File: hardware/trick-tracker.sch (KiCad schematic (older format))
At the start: 58 parts, among them J1 USB4105-GF-A, J2 S2B-PH-K, J3 QWiiC, J4 MEM2051-00-195-00-A, J6 QWiiC, P1 SMTB-1240-S-R, U1 MS88SF2, U2 DPS368XTSA1, U3 LSM9DS1, U4 MCP73831/OT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

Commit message: Finished trace routing
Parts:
- J4: value MEM2051-00-195-00-A -> MEM2061-01-188-00-A
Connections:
- no-connect marks 10 -> 9
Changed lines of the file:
@@
 Text Label 3400 6050 2    50   ~ 0
 D-
-NoConn ~ 3100 6450
 $Comp
 L power:GND #PWR0104
@@
 P 2150 4500
 F 0 "J4" H 2150 5067 50  0000 C CNN
-F 1 "MEM2051-00-195-00-A" H 2150 4976 50  0000 C CNN
+F 1 "MEM2061-01-188-00-A" H 2150 4976 50  0000 C CNN
 F 2 "MEM2061-01-188-00-A_REVA:GCT_MEM2061-01-188-00-A_REVA" H 2150 4500 50  0001 L BNN
 F 3 "" H 2150 4500 50  0001 L BNN

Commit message: Small adjustments + rounded corners + BOM HTML
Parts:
- H1, H2, H3, H4: footprint MountingHole:MountingHole_2.5mm -> MountingHole:MountingHole_2.5mm_Pad_Via
- J1: Alternative (none) -> TYPE-C-31-M-12; MANUFACTURER GCT -> (none); MAXIMUM_PACKAGE_HEIGHT 3.31 mm -> (none); PARTREV A3 -> (none); STANDARD Manufacturer Recommendations -> (none)
- J4: MANUFACTURER GCT -> (none)
- S1, S2: Arrow Part Number EVQ-PUA02K -> (none); Arrow Price/Stock https://www.arrow.com/en/products/evq-pua02k/panasonic -> (none); Height 1.95 -> (none); Manufacturer_Name Panasonic -> (none); Manufacturer_Part_Number EVQ-PUA02K -> (none); Mouser Part Number 667-EVQ-PUA02K -> (none); Mouser Price/Stock https://www.mouser.co.uk/ProductDetail/Panasonic/EVQ-PUA02K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 -> (none)
- S3: Manufacturer_Name Wurth Elektronik -> (none); Manufacturer_Part_Number 450405020524 -> (none); Mouser Part Number 710-450405020524 -> (none); Mouser Price/Stock https://www.mouser.co.uk/ProductDetail/Wurth-Elektronik/450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 -> (none)
- U2: Field4 Infineon Technologies -> (none); Field5 None -> (none); Field6 Unavailable -> (none); Field7 DPS368XTSA1 -> (none); Field8 Package dimensions: 8-pin LGA, 2.0 x 2.5 x 1.1 mm3 | Operat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 -> (none)
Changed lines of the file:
@@
 F 2 "DPS368XTSA1:XDCR_DPS368XTSA1" H 5600 4200 50  0001 L BNN
 F 3 "VFLGA-8 Infineon Technologies" H 5600 4200 50  0001 L BNN
-F 4 "Infineon Technologies" H 5600 4200 50  0001 L BNN "Field4"
-F 5 "None" H 5600 4200 50  0001 L BNN "Field5"
-F 6 "Unavailable" H 5600 4200 50  0001 L BNN "Field6"
-F 7 "DPS368XTSA1" H 5600 4200 50  0001 L BNN "Field7"
-F 8 "Package dimensions: 8-pin LGA, 2.0 x 2.5 x 1.1 mm3 | Operation range: Pressure: 3001200 hPa Temperature: -4085C | Precision: 0.002 hPa _or 0.02 m_ | Rel. accuracy: 0.06 hPa _or 0.5 m_ | Abs. accuracy: 1 hPa _or 8 m_ | Temperature accuracy: 0.5C | Avg. current consumption: 1.7 A_pressure measurement_ @1Hzsampling rate, standby: 0.5 A. | Integrated FIFO | Interface: I2C and SPI_both with optional interrupt_" H 5600 4200 50  0001 L BNN "Field8"
 	1    5600 4200
 	1    0    0    -1
@@
 F 2 "USB4105-GF-A:GCT_USB4105-GF-A" H 2300 6050 50  0001 L BNN
 F 3 "" H 2300 6050 50  0001 L BNN
-F 4 "A3" H 2300 6050 50  0001 L BNN "PARTREV"
-F 5 "3.31 mm" H 2300 6050 50  0001 L BNN "MAXIMUM_PACKAGE_HEIGHT"
-F 6 "Manufacturer Recommendations" H 2300 6050 50  0001 L BNN "STANDARD"
-F 7 "GCT" H 2300 6050 50  0001 L BNN "MANUFACTURER"
+F 4 "TYPE-C-31-M-12" H 2300 6100 50  0001 C CNN "Alternative"
 	1    2300 6050
 	1    0    0    -1
@@
 F 3 "https://www.mouser.in/ProductDetail/Panasonic/EVQ-PUA02K?qs=%2Fha2pyFadujMSX8lHuHLeTqtnZtxLpuLygd0%252BejhC2g%3D" H 6000 6750 50  0001 L CNN
 F 4 "Tactile Switches SIDE PUSH 2.2NF 4.7x3.2x1.65mm" H 6000 6650 50  0001 L CNN "Description"
-F 5 "1.95" H 6000 6550 50  0001 L CNN "Height"
-F 6 "Panasonic" H 6000 6450 50  0001 L CNN "Manufacturer_Name"
-F 7 "EVQ-PUA02K" H 6000 6350 50  0001 L CNN "Manufacturer_Part_Number"
-F 8 "667-EVQ-PUA02K" H 6000 6250 50  0001 L CNN "Mouser Part Number"
-F 9 "https://www.mouser.co.uk/ProductDetail/Panasonic/EVQ-PUA02K?qs=whhzBCqEXCvFsgipcL1tig%3D%3D" H 6000 6150 50  0001 L CNN "Mouser Price/Stock"
-F 10 "EVQ-PUA02K" H 6000 6050 50  0001 L CNN "Arrow Part Number"
-F 11 "https://www.arrow.com/en/products/evq-pua02k/panasonic" H 6000 5950 50  0001 L CNN "Arrow Price/Stock"
 	1    4950 6750
 	1    0    0    -1
@@
 F 3 "https://www.mouser.in/ProductDetail/Panasonic/EVQ-PUA02K?qs=%2Fha2pyFadujMSX8lHuHLeTqtnZtxLpuLygd0%252BejhC2g%3D" H 6000 7400 50  0001 L CNN
 F 4 "Tactile Switches SIDE PUSH 2.2NF 4.7x3.2x1.65mm" H 6000 7300 50  0001 L CNN "Description"
-F 5 "1.95" H 6000 7200 50  0001 L CNN "Height"
-F 6 "Panasonic" H 6000 7100 50  0001 L CNN "Manufacturer_Name"
-F 7 "EVQ-PUA02K" H 6000 7000 50  0001 L CNN "Manufacturer_Part_Number"
-F 8 "667-EVQ-PUA02K" H 6000 6900 50  0001 L CNN "Mouser Part Number"
-F 9 "https://www.mouser.co.uk/ProductDetail/Panasonic/EVQ-PUA02K?qs=whhzBCqEXCvFsgipcL1tig%3D%3D" H 6000 6800 50  0001 L CNN "Mouser Price/Stock"
-F 10 "EVQ-PUA02K" H 6000 6700 50  0001 L CNN "Arrow Part Number"
-F 11 "https://www.arrow.com/en/products/evq-pua02k/panasonic" H 6000 6600 50  0001 L CNN "Arrow Price/Stock"
 	1    4950 7400
 	1    0    0    -1
@@
 F 0 "H1" H 4650 5496 50  0000 L CNN
 F 1 "MountingHole" H 4650 5405 50  0000 L CNN
-F 2 "MountingHole:MountingHole_2.5mm" H 4550 5450 50  0001 C CNN
+F 2 "MountingHole:MountingHole_2.5mm_Pad_Via" H 4550 5450 50  0001 C CNN
 F 3 "~" H 4550 5450 50  0001 C CNN
 	1    4550 5450
@@
 F 0 "H2" H 4650 5746 50  0000 L CNN
 F 1 "MountingHole" H 4650 5655 50  0000 L CNN
-F 2 "MountingHole:MountingHole_2.5mm" H 4550 5700 50  0001 C CNN
+F 2 "MountingHole:MountingHole_2.5mm_Pad_Via" H 4550 5700 50  0001 C CNN
 F 3 "~" H 4550 5700 50  0001 C CNN
 	1    4550 5700
@@
 F 4 "Slide Switches WS-SLSU Mini Slide Switch" H 8800 4350 50  0001 L CNN "Description"
 F 5 "2.25" H 8800 4250 50  0001 L CNN "Height"
-F 6 "Wurth Elektronik" H 8800 4150 50  0001 L CNN "Manufacturer_Name"
-F 7 "450405020524" H 8800 4050 50  0001 L CNN "Manufacturer_Part_Number"
-F 8 "710-450405020524" H 8800 3950 50  0001 L CNN "Mouser Part Number"
-F 9 "https://www.mouser.co.uk/ProductDetail/Wurth-Elektronik/450405020524/?qs=OlC7AqGiEDnl%252BU2cnq%252B3rQ%3D%3D" H 8800 3850 50  0001 L CNN "Mouser Price/Stock"
-F 10 "" H 8800 3750 50  0001 L CNN "Arrow Part Number"
-F 11 "" H 8800 3650 50  0001 L CNN "Arrow Price/Stock"
 	1    7950 4450
 	1    0    0    -1
@@
 F 2 "MEM2061-01-188-00-A_REVA:GCT_MEM2061-01-188-00-A_REVA" H 2150 4500 50  0001 L BNN
 F 3 "" H 2150 4500 50  0001 L BNN
-F 4 "GCT" H 2150 4500 50  0001 L BNN "MANUFACTURER"
 	1    2150 4500
 	1    0    0    -1
@@
 F 0 "H3" H 4650 5996 50  0000 L CNN
 F 1 "MountingHole" H 4650 5905 50  0000 L CNN
-F 2 "MountingHole:MountingHole_2.5mm" H 4550 5950 50  0001 C CNN
+F 2 "MountingHole:MountingHole_2.5mm_Pad_Via" H 4550 5950 50  0001 C CNN
 F 3 "~" H 4550 5950 50  0001 C CNN
 	1    4550 5950
@@
 F 0 "H4" H 4650 6246 50  0000 L CNN
 F 1 "MountingHole" H 4650 6155 50  0000 L CNN
-F 2 "MountingHole:MountingHole_2.5mm" H 4550 6200 50  0001 C CNN
+F 2 "MountingHole:MountingHole_2.5mm_Pad_Via" H 4550 6200 50  0001 C CNN
 F 3 "~" H 4550 6200 50  0001 C CNN
 	1    4550 6200

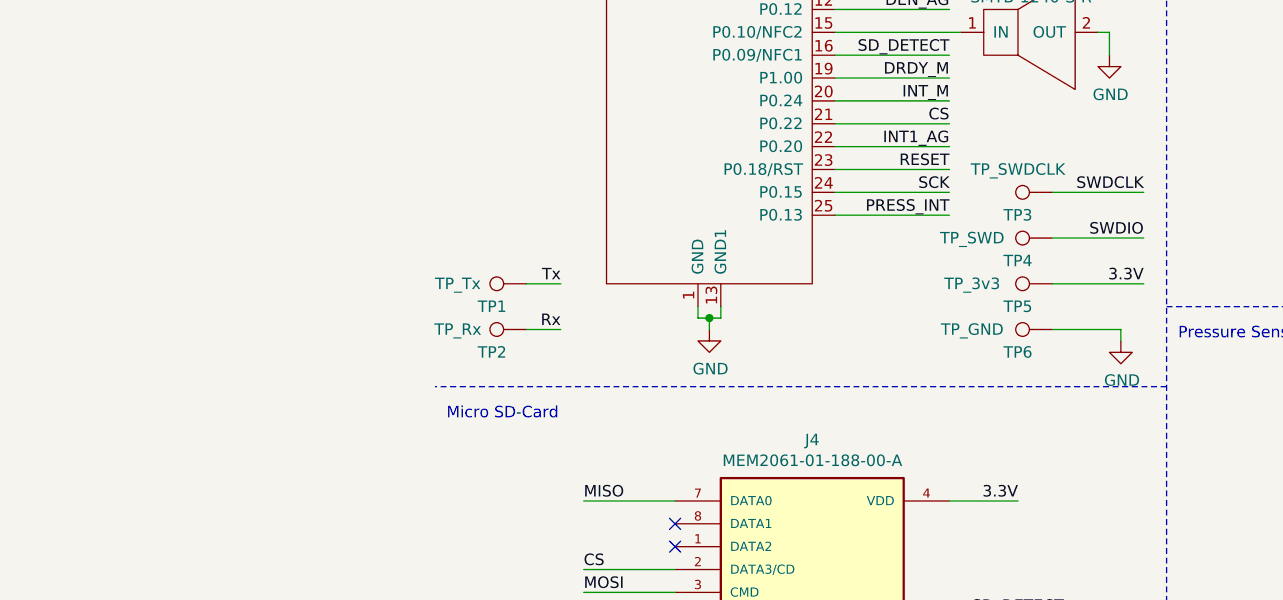
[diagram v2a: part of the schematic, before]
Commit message: Add connector (placeholder) + extra GND TP
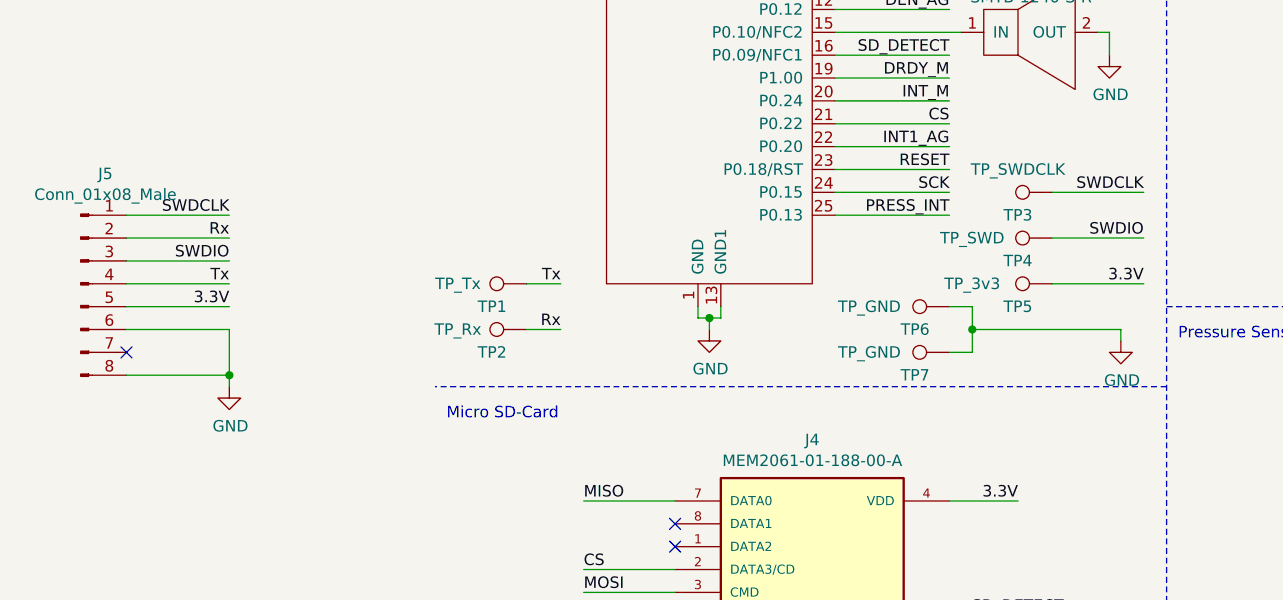
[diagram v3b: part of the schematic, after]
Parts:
- added J5: Conn_01x08_Male, Connector_PinSocket_2.54mm:PinSocket_2x04_P2.54mm_Vertical_SMD, symbol Connector:Conn_01x08_Male
- added TP7: TP_GND, TestPoint:TestPoint_Pad_D1.5mm, symbol Connector:TestPoint
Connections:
- net 3.3V: now also J5.5 (Pin_5)
- net GND: now also J5.6 (Pin_6), J5.8 (Pin_8), TP7.1
- net Rx: now also J5.2 (Pin_2)
- net SWDCLK: now also J5.1 (Pin_1)
- net SWDIO: now also J5.3 (Pin_3)
- net Tx: now also J5.4 (Pin_4)
- no-connect marks 9 -> 10
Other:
- moved on the sheet: TP6
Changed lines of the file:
@@
 Wire Wire Line
 	3500 3500 3500 3450
-Wire Wire Line
-	3500 3450 3200 3450
 $Comp
 L SMTB-1240-S-R:SMTB-1240-S-R P1
@@
 L Connector:TestPoint TP6
 U 1 1 60ADFDB3
-P 3200 3450
-F 0 "TP6" V 3100 3600 50  0000 C CNN
-F 1 "TP_GND" V 3200 3800 50  0000 C CNN
-F 2 "TestPoint:TestPoint_Pad_D1.5mm" H 3400 3450 50  0001 C CNN
-F 3 "~" H 3400 3450 50  0001 C CNN
-	1    3200 3450
+P 2750 3350
+F 0 "TP6" V 2650 3500 50  0000 C CNN
+F 1 "TP_GND" V 2750 3700 50  0000 C CNN
+F 2 "TestPoint:TestPoint_Pad_D1.5mm" H 2950 3350 50  0001 C CNN
+F 3 "~" H 2950 3350 50  0001 C CNN
+	1    2750 3350
 	0    -1   -1   0
 $EndComp
@@
 Wire Wire Line
 	1050 3450 900  3450
+$Comp
+L Connector:TestPoint TP7
+U 1 1 60B4C6F1
+P 2750 3550
+F 0 "TP7" V 2650 3700 50  0000 C CNN
+F 1 "TP_GND" V 2750 3900 50  0000 C CNN
+F 2 "TestPoint:TestPoint_Pad_D1.5mm" H 2950 3550 50  0001 C CNN
+F 3 "~" H 2950 3550 50  0001 C CNN
+	1    2750 3550
+	0    -1   -1   0
+$EndComp
+Wire Wire Line
+	2850 3450 2850 3550
+Wire Wire Line
+	2850 3550 2750 3550
+Wire Wire Line
+	2850 3450 3500 3450
+Wire Wire Line
+	2750 3350 2850 3350
+Wire Wire Line
+	2850 3350 2850 3450
+Connection ~ 2850 3450
+$Comp
+L Connector:Conn_01x08_Male J5
+U 1 1 60B6B637
+P -1050 3250
+F 0 "J5" H -942 3731 50  0000 C CNN
+F 1 "Conn_01x08_Male" H -942 3640 50  0000 C CNN
+F 2 "Connector_PinSocket_2.54mm:PinSocket_2x04_P2.54mm_Vertical_SMD" H -1050 3250 50  0001 C CNN
+F 3 "~" H -1050 3250 50  0001 C CNN
+	1    -1050 3250
+	1    0    0    -1
+$EndComp
+Text Label -400 2950 2    50   ~ 0
+SWDCLK
+Text Label -400 3150 2    50   ~ 0
+SWDIO
+Text Label -400 3350 2    50   ~ 0
+3.3V
+$Comp
+L power:GND #PWR0136
+U 1 1 60B7C7CE
+P -400 3700
+F 0 "#PWR0136" H -400 3450 50  0001 C CNN
+F 1 "GND" H -395 3527 50  0000 C CNN
+F 2 "" H -400 3700 50  0001 C CNN
+F 3 "" H -400 3700 50  0001 C CNN
+	1    -400 3700
+	1    0    0    -1
+$EndComp
+Text Label -400 3050 2    50   ~ 0
+Rx
+Text Label -400 3250 2    50   ~ 0
+Tx
+Wire Wire Line
+	-850 3450 -400 3450
+Wire Wire Line
+	-400 3450 -400 3650
+Wire Wire Line
+	-850 3650 -400 3650
+Connection ~ -400 3650
+Wire Wire Line
+	-400 3650 -400 3700
+Wire Wire Line
+	-400 2950 -850 2950
+Wire Wire Line
+	-850 3050 -400 3050
+Wire Wire Line
+	-400 3150 -850 3150
+Wire Wire Line
+	-850 3250 -400 3250
+Wire Wire Line
+	-400 3350 -850 3350
+NoConn ~ -850 3550
 $EndSCHEMATC

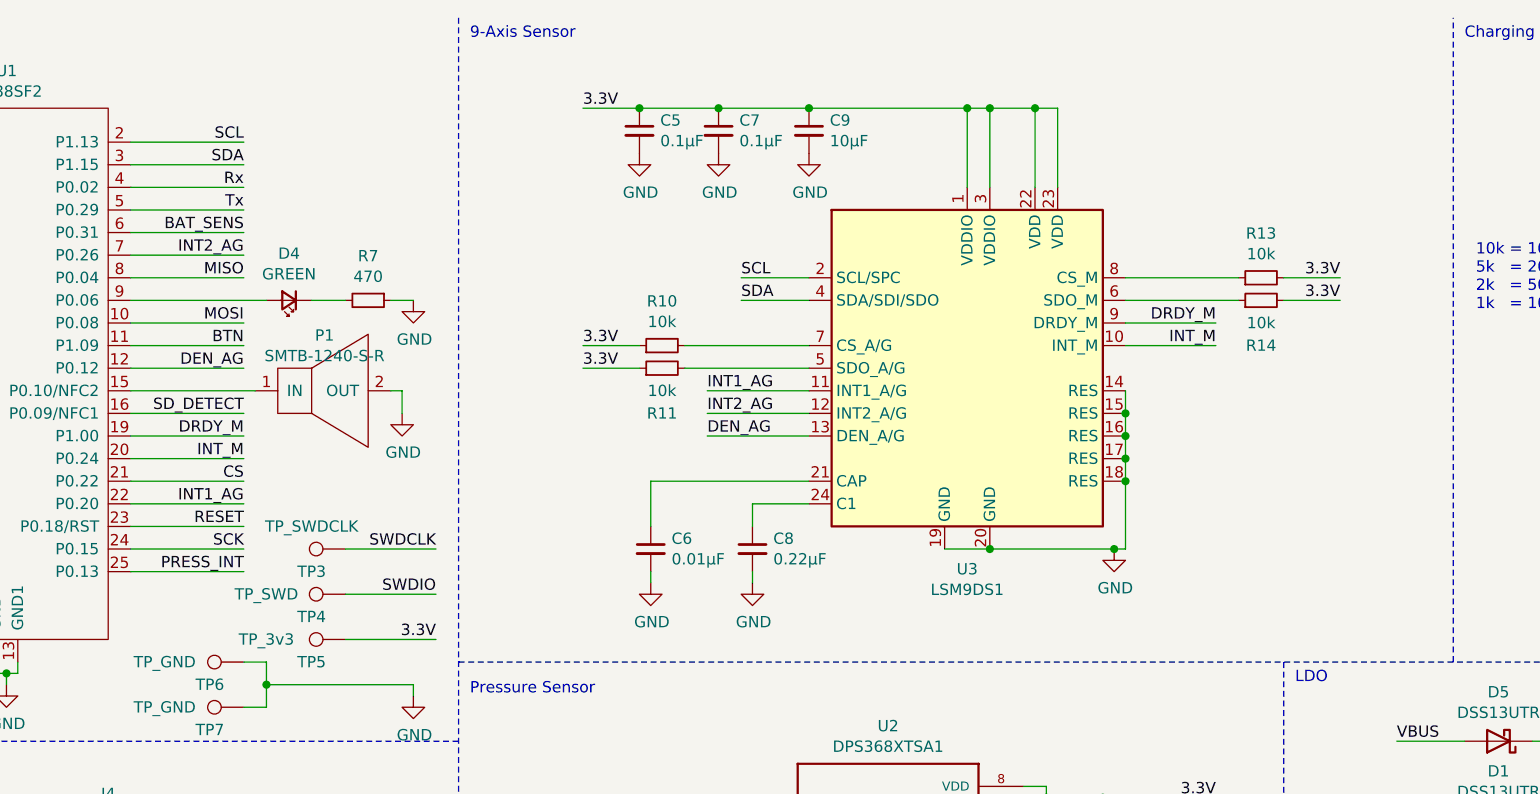
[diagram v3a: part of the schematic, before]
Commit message: Start layout BN055 sensor to replace the other accel sensor
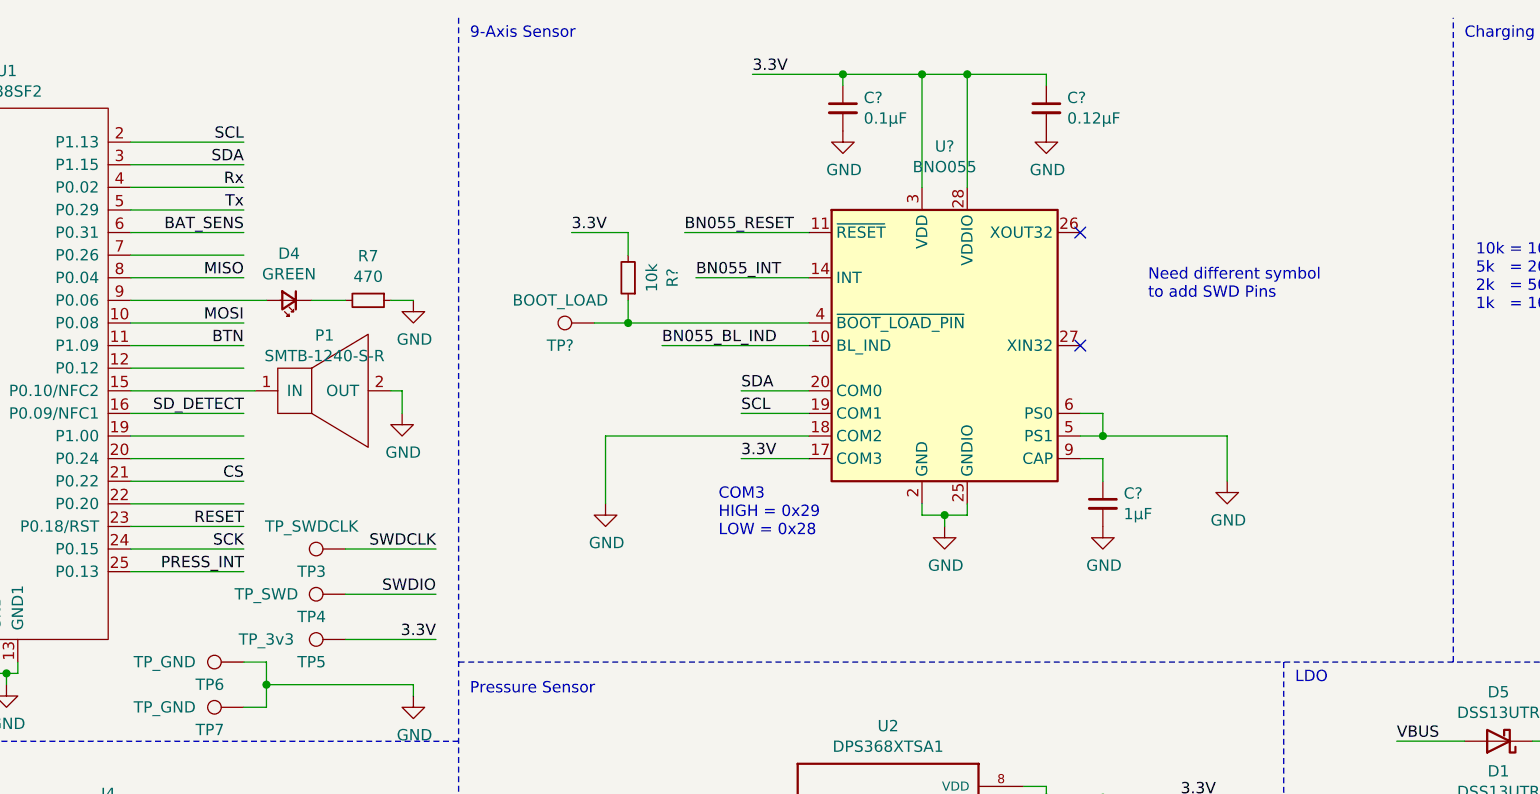
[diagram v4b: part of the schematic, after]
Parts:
- removed C5, C7: 0.1µF, Capacitor_SMD:C_0603_1608Metric, symbol Device:C_Small
- removed C6: 0.01µF, Capacitor_SMD:C_0603_1608Metric, symbol Device:C_Small
- removed C8: 0.22µF, Capacitor_SMD:C_0603_1608Metric, symbol Device:C_Small
- removed C9: 10µF, Capacitor_SMD:C_0603_1608Metric, symbol Device:C_Small
- removed R10, R11, R13, R14: 10k, Resistor_SMD:R_0603_1608Metric, symbol Device:R_Small
- removed U3: LSM9DS1, Package_LGA:LGA-24L_3x3.5mm_P0.43mm, symbol Sensor_Motion:LSM9DS1
- added C?: 0.12µF, Capacitor_SMD:C_0603_1608Metric, symbol Device:C_Small
- added C?: 0.1µF, Capacitor_SMD:C_0603_1608Metric, symbol Device:C_Small
- added C?: 1µF, Capacitor_SMD:C_0603_1608Metric, symbol Device:C_Small
- added R?: 10k, Resistor_SMD:R_0603_1608Metric, symbol Device:R_Small
- added TP?: BOOT_LOAD, TestPoint:TestPoint_Pad_D1.5mm, symbol Connector:TestPoint
- added U?: BNO055, Package_LGA:LGA-28_5.2x3.8mm_P0.5mm, symbol Sensor_Motion:BNO055
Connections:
- net 3.3V: now also C?.1, C?.1, R?.2, U?.17 (COM3), U?.28 (VDDIO), U?.3 (VDD)
- net GND: now also C?.2, C?.2, C?.2, U?.15 (GNDIO), U?.16 (GNDIO), U?.18 (COM2), U?.2 (GND), U?.25 (GNDIO), U?.5 (PS1), U?.6 (PS0)
- net SCL: now also U?.19 (COM1)
- net SDA: now also U?.20 (COM0)
- net DEN_AG: no longer names the net of U1.12 (P0.12)
- net DRDY_M: no longer names the net of U1.19 (P1.00)
- net INT1_AG: no longer names the net of U1.22 (P0.20)
- net INT2_AG: no longer names the net of U1.7 (P0.26)
- net INT_M: no longer names the net of U1.20 (P0.24)
- new net: R?.1, TP?.1, U?.4 (~BOOT_LOAD_PIN)
- new net: C?.1, U?.9 (CAP)
- new net BN055_BL_IND: U?.10 (BL_IND)
- new net BN055_INT: U?.14 (INT)
- new net BN055_RESET: U?.11 (~RESET)
- no-connect marks 10 -> 12
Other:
- note added: "COM3\nHIGH = 0x29\nLOW = 0x28"
- note added: "Need different symbol\nto add SWD Pins"
